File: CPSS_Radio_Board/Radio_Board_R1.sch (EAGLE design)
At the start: 46 parts, among them IC1 FT2232D, T1 BCW81SMD, X1 BU-SMA-V, X2 MINI-USB-UX60-MB-5S8

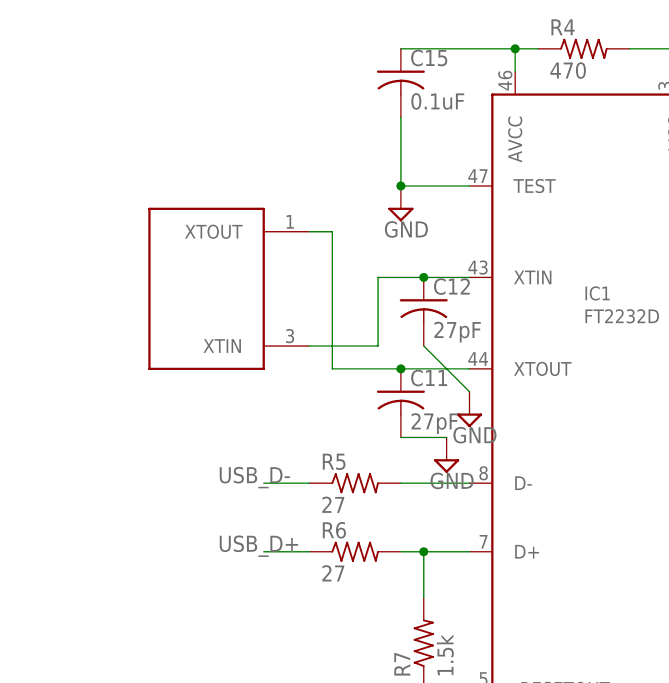
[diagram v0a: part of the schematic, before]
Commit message: Added BOM and PCB GND connections for crystal
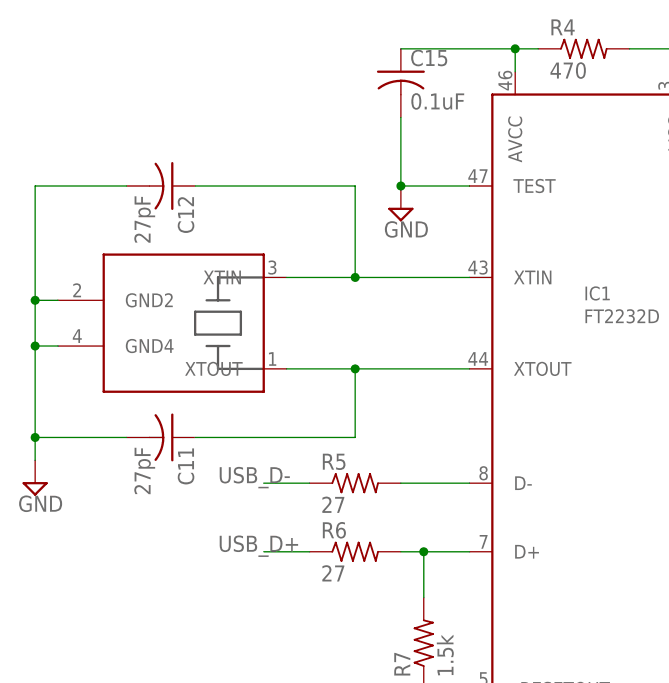
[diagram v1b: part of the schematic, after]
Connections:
- net GND: now also U$8.GND2, U$8.GND4
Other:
- moved on the sheet: C11, C12
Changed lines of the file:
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@@
 <part name="P+7" library="supply1" library_urn="urn:adsk.eagle:library:371" deviceset="+5V" device=""/>
 <part name="R2" library="resistor" library_urn="urn:adsk.eagle:library:348" deviceset="R-US_" device="R0805" package3d_urn="urn:adsk.eagle:package:26059/1" value="10k"/>
-<part name="U$8" library="ABMM_Crystal" deviceset="ABBM-6" device=""/>
 <part name="C11" library="resistor" library_urn="urn:adsk.eagle:library:348" deviceset="C-US" device="C0603" package3d_urn="urn:adsk.eagle:package:26138/1" value="27pF"/>
 <part name="C12" library="resistor" library_urn="urn:adsk.eagle:library:348" deviceset="C-US" device="C0603" package3d_urn="urn:adsk.eagle:package:26138/1" value="27pF"/>
+<part name="U$8" library="ABMM_Crystal" deviceset="ABBM-6" device=""/>
 <part name="SUPPLY5" library="supply2" library_urn="urn:adsk.eagle:library:372" deviceset="GND" device=""/>
-<part name="SUPPLY13" library="supply2" library_urn="urn:adsk.eagle:library:372" deviceset="GND" device=""/>
 </parts>
 <sheets>
@@
 <instance part="P+7" gate="1" x="30.48" y="-134.62"/>
 <instance part="R2" gate="G$1" x="12.7" y="-137.16" rot="R90"/>
-<instance part="U$8" gate="G$1" x="-40.64" y="-63.5" rot="MR0"/>
-<instance part="C11" gate="G$1" x="-17.78" y="-73.66"/>
-<instance part="C12" gate="G$1" x="-15.24" y="-63.5"/>
-<instance part="SUPPLY5" gate="GND" x="-10.16" y="-76.2"/>
-<instance part="SUPPLY13" gate="GND" x="-12.7" y="-81.28"/>
+<instance part="C11" gate="G$1" x="-43.18" y="-78.74" rot="R270"/>
+<instance part="C12" gate="G$1" x="-43.18" y="-50.8" rot="R270"/>
+<instance part="U$8" gate="G$1" x="-43.18" y="-66.04"/>
+<instance part="SUPPLY5" gate="GND" x="-58.42" y="-83.82"/>
 </instances>
 <busses>
@@
 </segment>
 <segment>
+<pinref part="U$8" gate="G$1" pin="GND2"/>
+<wire x1="-55.88" y1="-63.5" x2="-58.42" y2="-63.5" width="0.1524" layer="91"/>
+<wire x1="-58.42" y1="-63.5" x2="-58.42" y2="-50.8" width="0.1524" layer="91"/>
 <pinref part="C12" gate="G$1" pin="2"/>
+<wire x1="-58.42" y1="-50.8" x2="-48.26" y2="-50.8" width="0.1524" layer="91"/>
+<wire x1="-58.42" y1="-63.5" x2="-58.42" y2="-68.58" width="0.1524" layer="91"/>
+<junction x="-58.42" y="-63.5"/>
+<pinref part="U$8" gate="G$1" pin="GND4"/>
+<wire x1="-58.42" y1="-68.58" x2="-55.88" y2="-68.58" width="0.1524" layer="91"/>
+<wire x1="-58.42" y1="-68.58" x2="-58.42" y2="-78.74" width="0.1524" layer="91"/>
+<junction x="-58.42" y="-68.58"/>
+<pinref part="C11" gate="G$1" pin="2"/>
+<wire x1="-58.42" y1="-78.74" x2="-48.26" y2="-78.74" width="0.1524" layer="91"/>
 <pinref part="SUPPLY5" gate="GND" pin="GND"/>
-<wire x1="-10.16" y1="-73.66" x2="-15.24" y2="-68.58" width="0.1524" layer="91"/>
-</segment>
-<segment>
-<pinref part="C11" gate="G$1" pin="2"/>
-<pinref part="SUPPLY13" gate="GND" pin="GND"/>
-<wire x1="-12.7" y1="-78.74" x2="-17.78" y2="-78.74" width="0.1524" layer="91"/>
+<wire x1="-58.42" y1="-81.28" x2="-58.42" y2="-78.74" width="0.1524" layer="91"/>
+<junction x="-58.42" y="-78.74"/>
 </segment>
 </net>
@@
 <net name="N$3" class="0">
 <segment>
+<pinref part="IC1" gate="G$1" pin="XTIN"/>
 <pinref part="U$8" gate="G$1" pin="XTIN"/>
-<wire x1="-27.94" y1="-68.58" x2="-20.32" y2="-68.58" width="0.1524" layer="91"/>
-<wire x1="-20.32" y1="-68.58" x2="-20.32" y2="-60.96" width="0.1524" layer="91"/>
-<pinref part="IC1" gate="G$1" pin="XTIN"/>
-<wire x1="-20.32" y1="-60.96" x2="-15.24" y2="-60.96" width="0.1524" layer="91"/>
+<wire x1="-10.16" y1="-60.96" x2="-22.86" y2="-60.96" width="0.1524" layer="91"/>
 <pinref part="C12" gate="G$1" pin="1"/>
-<wire x1="-15.24" y1="-60.96" x2="-10.16" y2="-60.96" width="0.1524" layer="91"/>
-<junction x="-15.24" y="-60.96"/>
+<wire x1="-22.86" y1="-60.96" x2="-30.48" y2="-60.96" width="0.1524" layer="91"/>
+<wire x1="-40.64" y1="-50.8" x2="-22.86" y2="-50.8" width="0.1524" layer="91"/>
+<wire x1="-22.86" y1="-50.8" x2="-22.86" y2="-60.96" width="0.1524" layer="91"/>
+<junction x="-22.86" y="-60.96"/>
 </segment>
 </net>
@@
 <segment>
 <pinref part="U$8" gate="G$1" pin="XTOUT"/>
-<wire x1="-27.94" y1="-55.88" x2="-25.4" y2="-55.88" width="0.1524" layer="91"/>
-<wire x1="-25.4" y1="-55.88" x2="-25.4" y2="-71.12" width="0.1524" layer="91"/>
 <pinref part="IC1" gate="G$1" pin="XTOUT"/>
-<wire x1="-25.4" y1="-71.12" x2="-17.78" y2="-71.12" width="0.1524" layer="91"/>
+<wire x1="-30.48" y1="-71.12" x2="-22.86" y2="-71.12" width="0.1524" layer="91"/>
 <pinref part="C11" gate="G$1" pin="1"/>
-<wire x1="-17.78" y1="-71.12" x2="-10.16" y2="-71.12" width="0.1524" layer="91"/>
-<junction x="-17.78" y="-71.12"/>
-</segment>
-</net>
+<wire x1="-22.86" y1="-71.12" x2="-10.16" y2="-71.12" width="0.1524" layer="91"/>
+<wire x1="-40.64" y1="-78.74" x2="-22.86" y2="-78.74" width="0.1524" layer="91"/>
+<wire x1="-22.86" y1="-78.74" x2="-22.86" y2="-71.12" width="0.1524" layer="91"/>
+<junction x="-22.86" y="-71.12"/>
+</segment>
+</net>
